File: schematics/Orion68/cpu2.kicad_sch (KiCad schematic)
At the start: 40 parts, among them J10 Conn_02x08_Counter_Clockwise, J6 systemTickFreq, J600 Euro96pin, J601 clock, J602 clock1, Q7 2N3904, Q8 2N3904, SW3 Reset, U16 74LS139, U2.? ICM7555xB, U21 74LS20, U22 74HC164, U24 74HC4078, U600 68000D, U601 74LS393, U602 74HC74, U603 74HC14, U604 ATmega8-16P

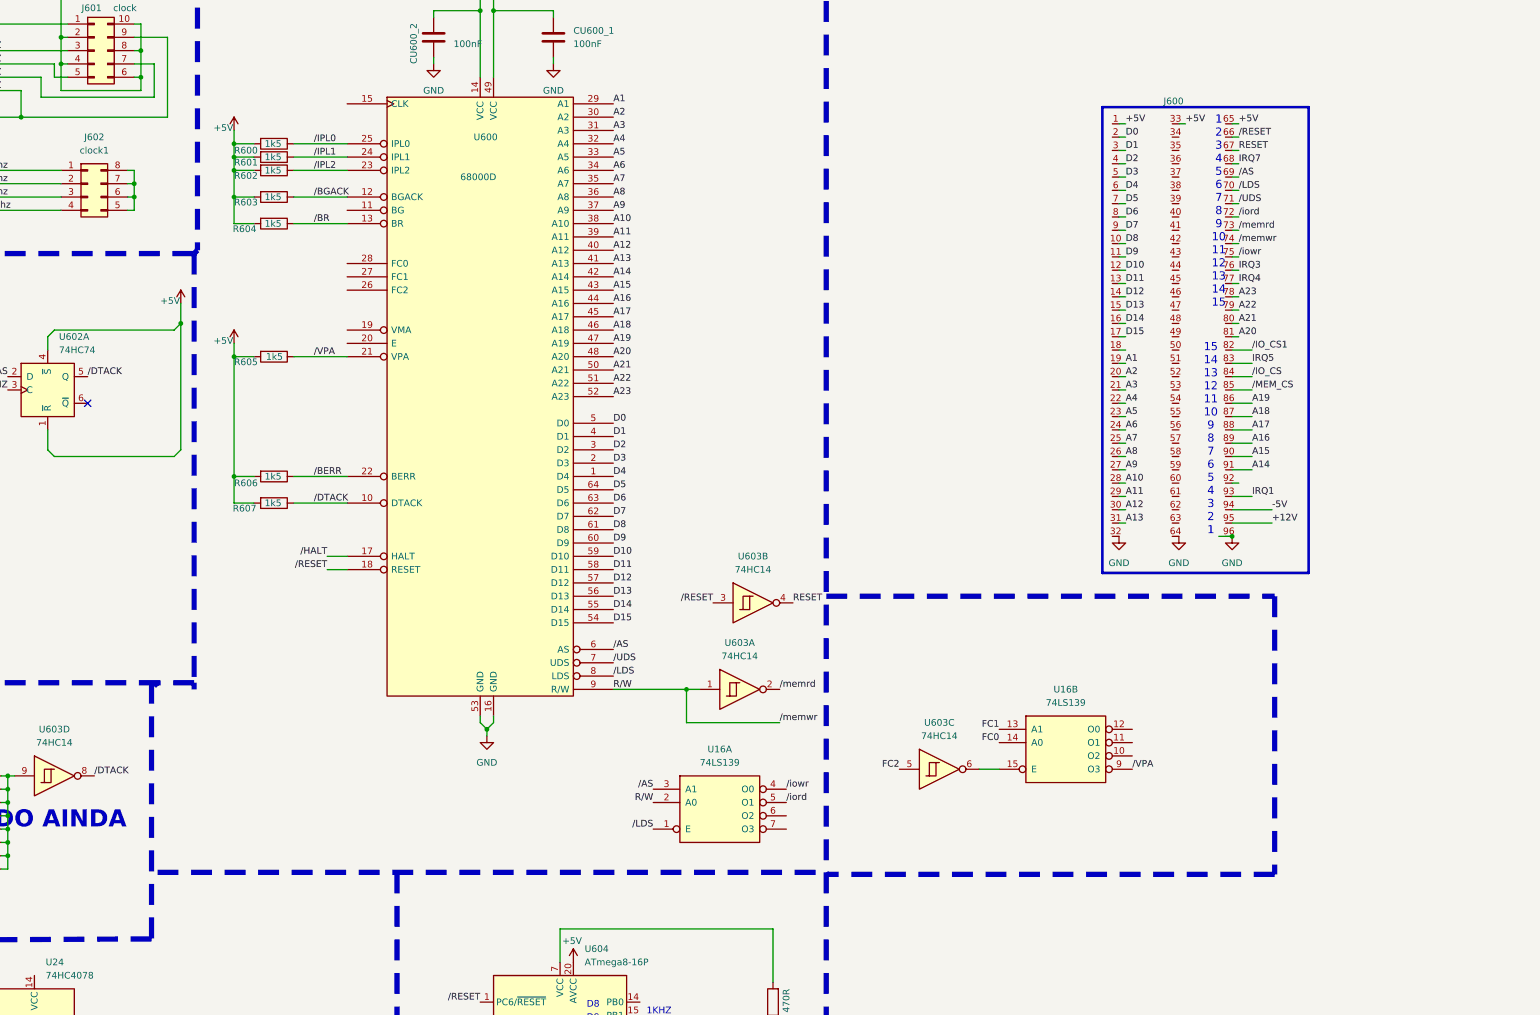
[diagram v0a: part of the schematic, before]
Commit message: Changed dtack system
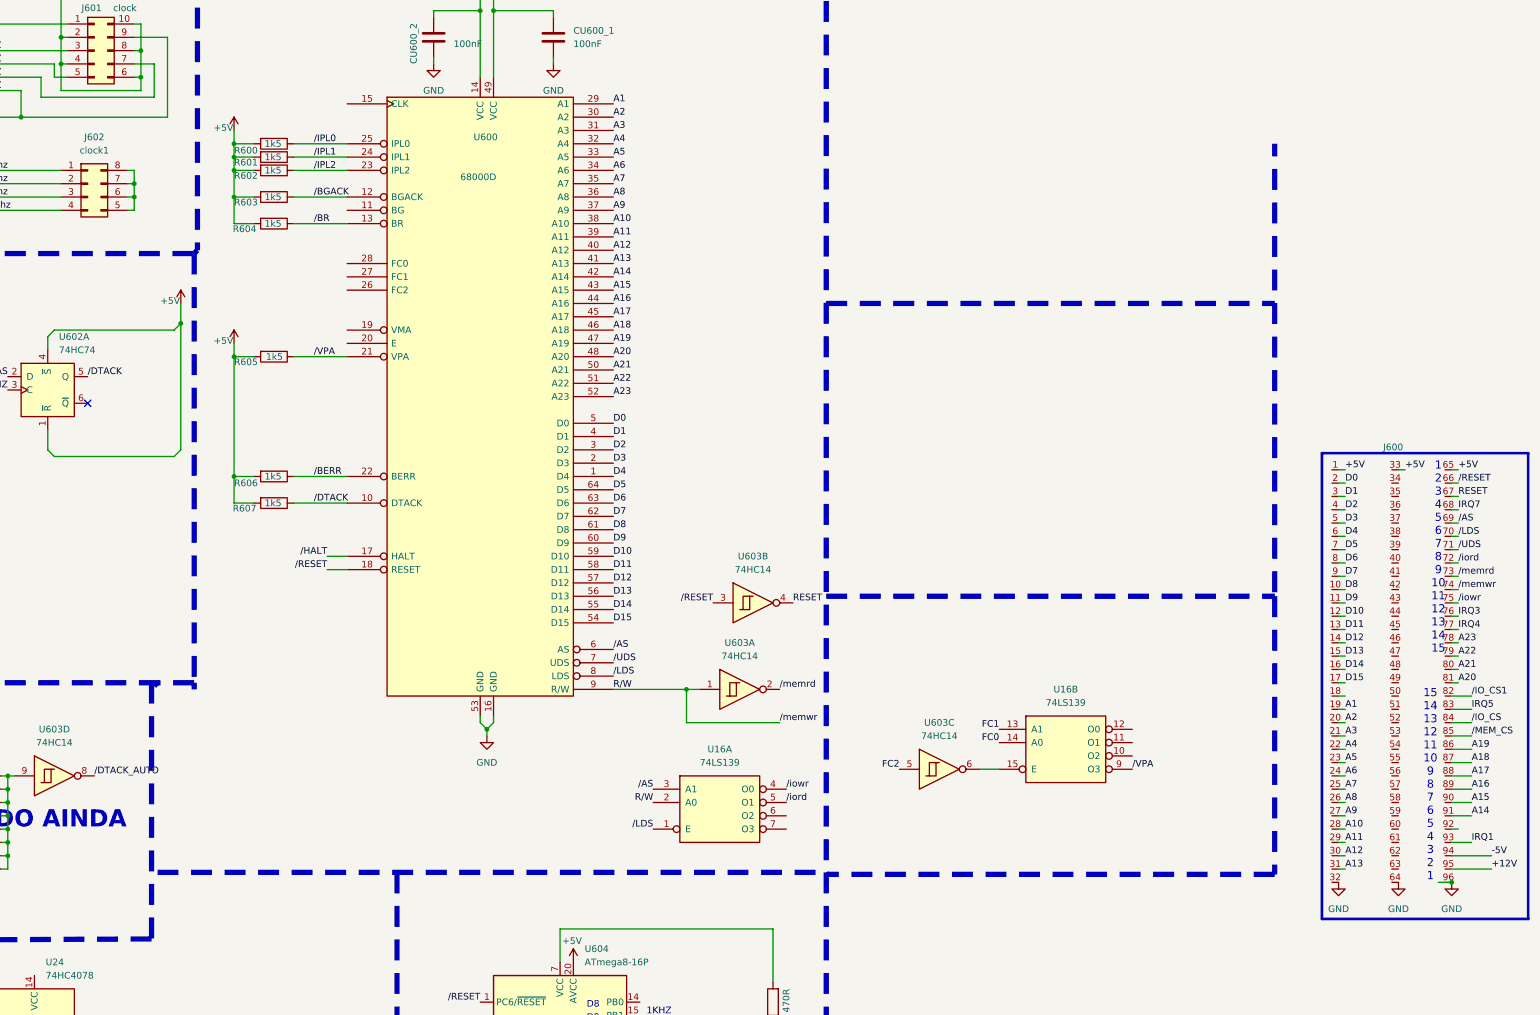
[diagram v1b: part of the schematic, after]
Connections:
- net /DTACK: no longer U603.8
- new net /DTACK_AUTO: U603.8
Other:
- moved on the sheet: J600

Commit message: Implemented new picoVGA V2
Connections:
- net /DTACK_AUTO: now also J600.62
- net /DTACK_PVGA: now reaches J600.59
- net /CS_MULTIO: now reaches J600.60
- net /DTACK_MIO: now reaches J600.61
- net /DTACK_CPU: now reaches J600.63
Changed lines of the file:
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@@
 	(wire
 		(pts
+			(xy 374.65 180.34) (xy 374.65 200.66)
+		)
+		(stroke
+			(width 0)
+			(type default)
+		)
+	)
+	(wire
+		(pts
 			(xy 71.12 109.22) (xy 71.12 116.84)
 		)
@@
 		)
 	)
+	(wire
+		(pts
+			(xy 374.65 180.34) (xy 378.46 180.34)
+		)
+		(stroke
+			(width 0)
+			(type default)
+		)
+	)
 	(polyline
 		(pts
@@
 	(wire
 		(pts
+			(xy 375.92 182.88) (xy 375.92 203.2)
+		)
+		(stroke
+			(width 0)
+			(type default)
+		)
+	)
+	(wire
+		(pts
 			(xy 76.2 91.44) (xy 74.93 91.44)
 		)
@@
 	(wire
 		(pts
+			(xy 372.11 175.26) (xy 378.46 175.26)
+		)
+		(stroke
+			(width 0)
+			(type default)
+		)
+	)
+	(wire
+		(pts
 			(xy 146.05 78.74) (xy 146.05 102.87)
 		)
@@
 	(wire
 		(pts
+			(xy 370.84 195.58) (xy 372.11 195.58)
+		)
+		(stroke
+			(width 0)
+			(type default)
+		)
+	)
+	(wire
+		(pts
 			(xy 156.21 59.69) (xy 160.02 59.69)
 		)
@@
 	(wire
 		(pts
+			(xy 378.46 172.72) (xy 381 172.72)
+		)
+		(stroke
+			(width 0)
+			(type default)
+		)
+	)
+	(wire
+		(pts
 			(xy 99.06 172.72) (xy 97.79 172.72)
 		)
@@
 	(wire
 		(pts
+			(xy 373.38 198.12) (xy 373.38 177.8)
+		)
+		(stroke
+			(width 0)
+			(type default)
+		)
+	)
+	(wire
+		(pts
 			(xy 78.74 39.37) (xy 78.74 49.53)
 		)
@@
 	(wire
 		(pts
+			(xy 373.38 177.8) (xy 378.46 177.8)
+		)
+		(stroke
+			(width 0)
+			(type default)
+		)
+	)
+	(wire
+		(pts
 			(xy 194.31 19.05) (xy 203.2 19.05)
 		)
@@
 		)
 	)
+	(wire
+		(pts
+			(xy 375.92 182.88) (xy 378.46 182.88)
+		)
+		(stroke
+			(width 0)
+			(type default)
+		)
+	)
 	(polyline
 		(pts
@@
 	(wire
 		(pts
+			(xy 370.84 200.66) (xy 374.65 200.66)
+		)
+		(stroke
+			(width 0)
+			(type default)
+		)
+	)
+	(wire
+		(pts
+			(xy 370.84 198.12) (xy 373.38 198.12)
+		)
+		(stroke
+			(width 0)
+			(type default)
+		)
+	)
+	(wire
+		(pts
 			(xy 76.2 172.72) (xy 76.2 175.26)
 		)
@@
 	(wire
 		(pts
+			(xy 381 172.72) (xy 381 195.58)
+		)
+		(stroke
+			(width 0)
+			(type default)
+		)
+	)
+	(wire
+		(pts
 			(xy 217.17 27.94) (xy 217.17 29.21)
 		)
@@
 	(wire
 		(pts
+			(xy 381 195.58) (xy 384.81 195.58)
+		)
+		(stroke
+			(width 0)
+			(type default)
+		)
+	)
+	(wire
+		(pts
 			(xy 99.06 182.88) (xy 97.79 182.88)
 		)
@@
 	(wire
 		(pts
+			(xy 370.84 203.2) (xy 375.92 203.2)
+		)
+		(stroke
+			(width 0)
+			(type default)
+		)
+	)
+	(wire
+		(pts
 			(xy 115.57 34.29) (xy 106.68 34.29)
 		)
@@
 	(wire
 		(pts
+			(xy 372.11 195.58) (xy 372.11 175.26)
+		)
+		(stroke
+			(width 0)
+			(type default)
+		)
+	)
+	(wire
+		(pts
 			(xy 368.3 132.08) (xy 367.03 132.08)
 		)
@@
 		)
 	)
+	(label "{slash}DTACK_MIO"
+		(at 370.84 198.12 180)
+		(effects
+			(font
+				(size 1.27 1.27)
+			)
+			(justify right bottom)
+		)
+	)
 	(label "A16"
 		(at 228.6 74.93 0)
@@
 		)
 	)
+	(label "{slash}DTACK_PVGA"
+		(at 384.81 195.58 0)
+		(effects
+			(font
+				(size 1.27 1.27)
+			)
+			(justify left bottom)
+		)
+	)
 	(label "D0"
 		(at 368.3 109.22 0)
@@
 		)
 	)
+	(label "{slash}CS_MULTIO"
+		(at 370.84 195.58 180)
+		(effects
+			(font
+				(size 1.27 1.27)
+			)
+			(justify right bottom)
+		)
+	)
 	(label "IRQ4"
 		(at 233.68 256.54 0)
@@
 		)
 	)
+	(label "{slash}DTACK_CPU"
+		(at 370.84 203.2 180)
+		(effects
+			(font
+				(size 1.27 1.27)
+			)
+			(justify right bottom)
+		)
+	)
 	(label "D11"
 		(at 228.6 125.73 0)
@@
 		)
 	)
+	(label "{slash}DTACK_AUTO"
+		(at 370.84 200.66 180)
+		(effects
+			(font
+				(size 1.27 1.27)
+			)
+			(justify right bottom)
+		)
+	)
